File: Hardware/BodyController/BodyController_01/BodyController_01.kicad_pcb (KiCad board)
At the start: 4 copper layers, 155 x 106 mm, 407 parts, among them J1 7796, J10 Conn_01x01, J11 Conn_01x01, J12 Conn_01x01, J13 Conn_01x01, J2 Conn_01x14, J3 Conn_02x10_Top_Bottom, J4 Conn_02x10_Top_Bottom, J5 7796, J6 7796, J7 CONN_01X06, J8 USB_OTG, J9 Conn_01x01, Q1 NX1029X,115, Q10 NX1029X,115, Q12 BUK9Y3R0-40E,115, Q13 BUK9Y3R0-40E,115, Q16 2N7002, Q17 Q_PMOS_GSD, Q2 NX1029X,115, Q3 2N7002, Q4 SQJ423EP-T1_GE3, Q6 NX1029X,115, Q7 NX1029X,115, Q8 2N7002, Q9 2N7002, SW1 PTS645SM43SMTR92 LFS, U1 PIC33EPxxxMU810, U10 LM2904AVQDRQ1, U11 BTS50202EKAXUMA2, U12 BTS50202EKAXUMA2, U13 BTS50202EKAXUMA2, U14 OPA320-Q1, U15 BTS716G, U16 MCP2562-H/SN, U17 TPS70950QDBVRQ1, U18 TPS70933QDBVRQ1, U19 TPS70933QDBVRQ1, U2 LM2903QDRQ1, U20 LMR140x0, U21 LM2903QDRQ1, U22 DRV8872DDARQ1, U23 tps25940-q1, U25 UCC27511A-Q1, U27 INA21x, U29 FT230X, U3 INA21x, U4 BTS716G, U5 BTS500801TMAATMA1, U6 BTS500801TMAATMA1, U7 BTS50202EKAXUMA2, U8 BTS50202EKAXUMA2, U9 BTS50202EKAXUMA2, Y1 8MHz

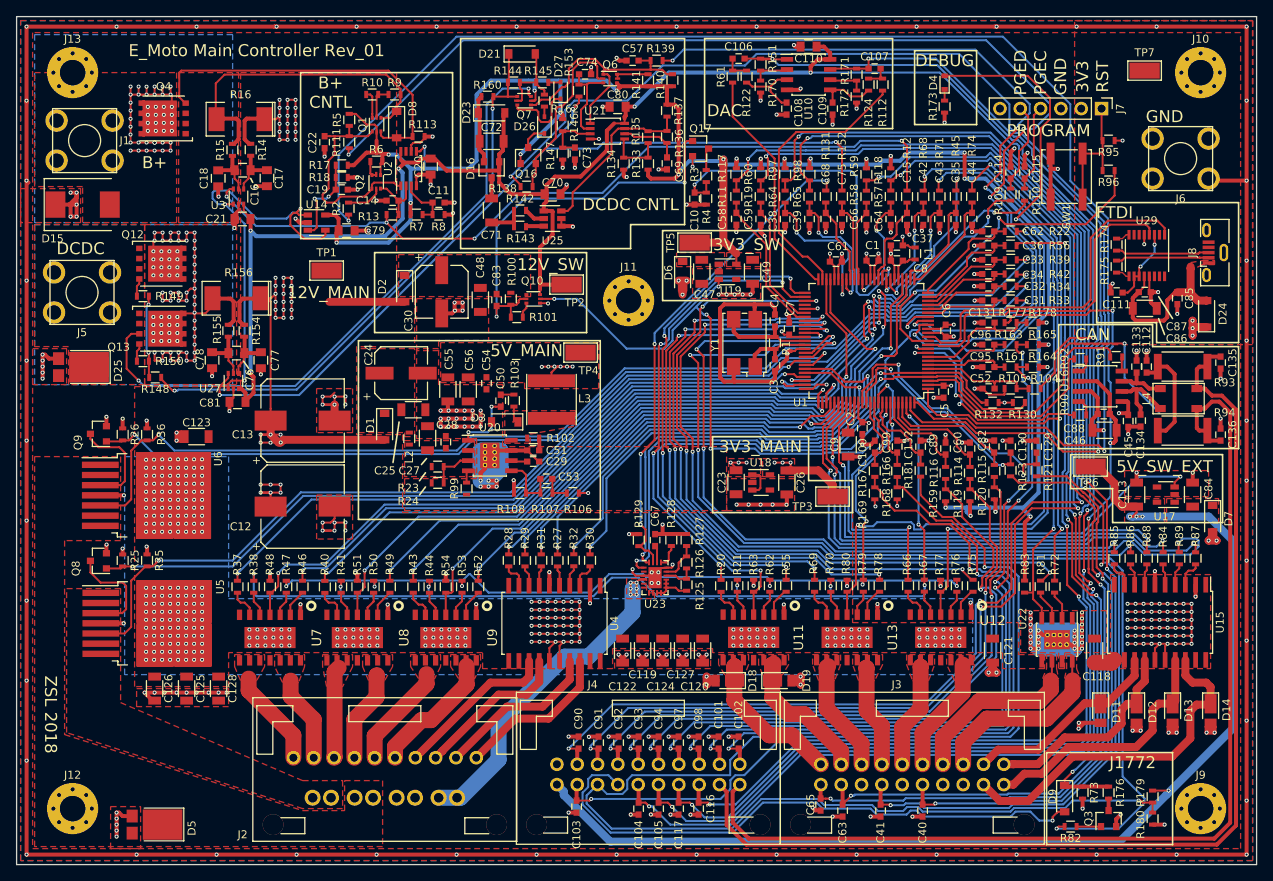
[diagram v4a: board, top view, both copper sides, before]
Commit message: Updated footprints, added CAN esd protection
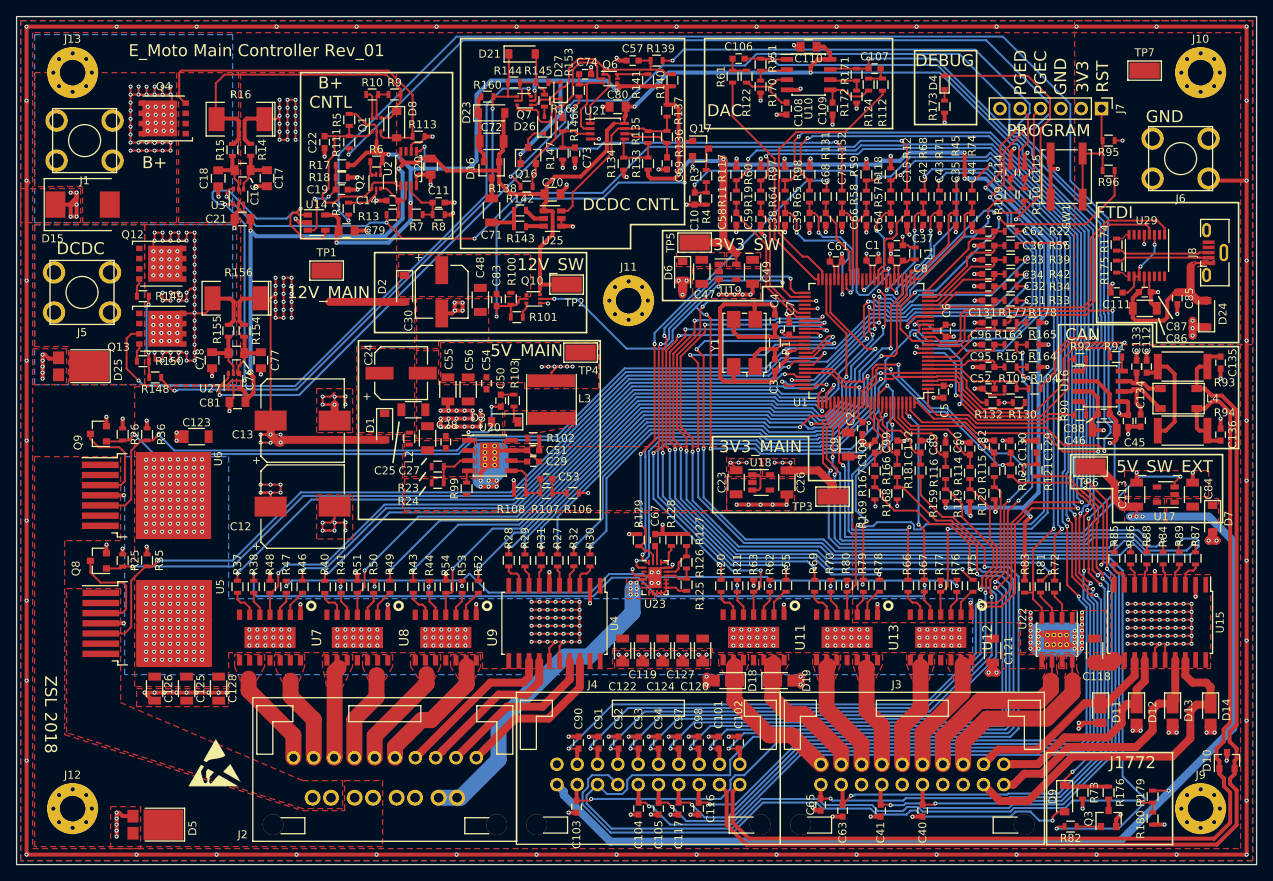
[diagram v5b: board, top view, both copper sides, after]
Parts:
- added D10: D_Schottky_x2_ACom_AKK, Footprints:D_SOT-23_ANK, F.Cu at (186.3, 150.0)
- added REF***: ESD-Logo_6.6x6mm_SilkScreen, Symbols:ESD-Logo_6.6x6mm_SilkScreen, F.Cu at (59.8, 150.2)
- Q12, Q13: value BUK9Y3R0-40E,115 -> BUK7J1R4-40HX
- moved D5 3.71 mm to (53.0, 158.0)
- moved D25 3.58 mm to (43.7, 100.7)
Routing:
- net (no net): track 22.5 -> 0.00 mm, vias 2 -> 0
- net +3V3: track 43.1 -> 64.3 mm, vias 16 -> 18
- net USB_5V: track 22.3 -> 24.8 mm
- net GND: track 986.5 -> 988.8 mm, vias 315 -> 316
- net CAN_P: track 135.7 -> 137.1 mm
- net CAN_N: track 132.1 -> 133.5 mm
- net BATT_EN: track 182.4 -> 183.4 mm

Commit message: Final layout for real this time. larger vias for EuroCircuit minimum rule.
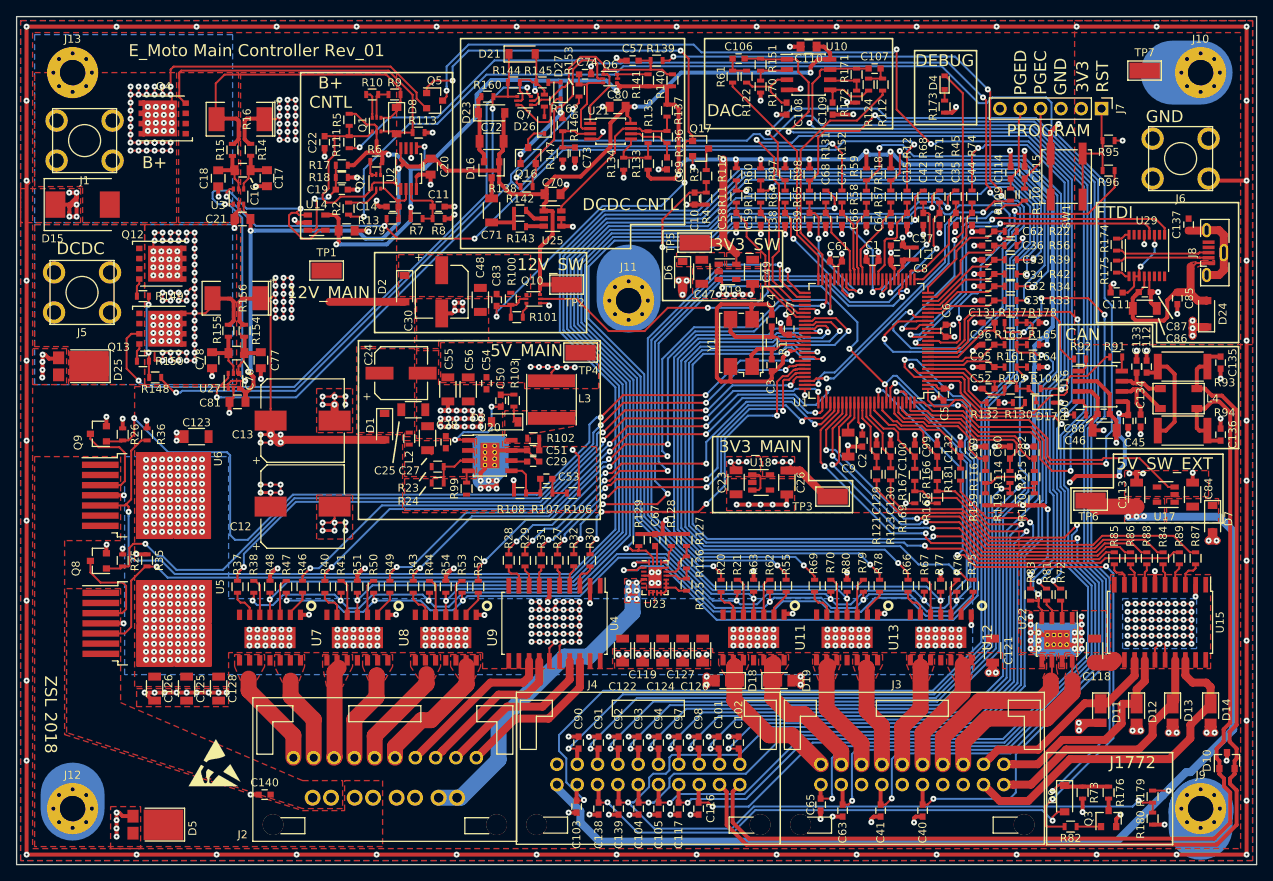
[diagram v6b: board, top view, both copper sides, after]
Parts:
- added C137: 10nF, Capacitors_SMD:C_0603, F.Cu at (181.5, 83.0)
- added C138: 10nF, Capacitors_SMD:C_0603, F.Cu at (107.8, 156.0)
- added C139: 10nF, Capacitors_SMD:C_0603, F.Cu at (110.2, 156.0)
- added C140: 10nF, Capacitors_SMD:C_0603, F.Cu at (66.0, 154.2)
- added D17: D_Schottky, Diodes_SMD:D_SOD-323, F.Cu at (163.5, 105.2)
- added Q5: Q_PMOS_GSD, TO_SOT_Packages_SMD:SOT-23, F.Cu at (87.2, 67.5)
- J10, J11, J12, J13, J9: footprint Mounting_Holes:MountingHole_3.2mm_M3_Pad_Via -> Footprints:MountingHole_3.2mm_M3_Pad_Via
- U2, U21: footprint Housings_SSOP:TSSOP-8_3x3mm_Pitch0.65mm -> Footprints:TSSOP-8_3x4.4mm_Pitch0.65mm
- moved C129 20.0 mm to (142.5, 111.2)
- moved R121 20.0 mm to (142.5, 114.2)
- moved C130 15.0 mm to (144.2, 111.2)
- moved R123 15.0 mm to (144.2, 114.2)
- moved C82 5.06 mm to (162.2, 111.5)
- moved R115 5.06 mm to (162.2, 114.5)
- moved R120 5.06 mm to (162.2, 117.3)
- moved C100 5.02 mm to (147.3, 111.3)
- moved C132 5.02 mm to (153.0, 111.2)
- moved C60 5.02 mm to (159.2, 111.5)
- moved C89 5.02 mm to (156.1, 111.5)
- moved C99 5.02 mm to (150.1, 111.2)
- moved R114 5.02 mm to (159.2, 114.5)
- moved R116 5.02 mm to (156.1, 114.5)
- moved R119 5.02 mm to (159.2, 117.3)
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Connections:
- J10 pad 1: Net-(J10-Pad1) -> GND
- J11 pad 1: Net-(J11-Pad1) -> GND
- J12 pad 1: Net-(J12-Pad1) -> GND
- J13 pad 1: Net-(J13-Pad1) -> GND
- J4 pad 13: PROXIMITY -> PILOT
- J4 pad 14: PILOT -> PROXIMITY
- J8 pad 6: GND -> Net-(C137-Pad1)
- J9 pad 1: Net-(J9-Pad1) -> GND
- R104 pad 1: +12P -> Net-(Q5-Pad3)
- U1 pad 59: PILOT_EN -> J1772_CONTROLLER_EN
- U1 pad 68: AUX_PORT_EN -> HORN_EN
- U1 pad 69: HORN_EN -> AUX_PORT_EN
- U1 pad 91: J1772_CONTROLLER_EN -> PILOT_EN
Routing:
- net Net-(Q5-Pad3): track 0.00 -> 124.6 mm, vias 0 -> 4
- net Net-(R34-Pad1): track 133.9 -> 201.7 mm
- net +12P: track 221.9 -> 155.4 mm, vias 6 -> 5
- net PILOT_EN: track 142.5 -> 85.1 mm
- net Net-(R33-Pad1): track 137.9 -> 193.0 mm
- net GND: track 988.8 -> 1040.0 mm, vias 316 -> 312
- net Net-(R68-Pad1): track 81.6 -> 126.3 mm
- net J1772_CONTROLLER_EN: track 36.9 -> 79.3 mm
- net Net-(R42-Pad1): track 110.5 -> 152.7 mm, vias 4 -> 2
- net Net-(R39-Pad1): track 121.3 -> 163.0 mm, vias 4 -> 2
- net DIVIDER_EN: track 50.1 -> 91.1 mm, vias 2 -> 4
- net +BATT: track 29.8 -> 66.7 mm
- net IC_CONTROLLER_SLEEP: track 72.6 -> 105.5 mm
- net IC_CONTROLLER_~FLT: track 66.4 -> 96.4 mm
- net CHARGE_PORT_RELEASE_EN: track 92.7 -> 120.0 mm, vias 4 -> 2
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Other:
- net class 5A: via_dia 0.5 -> 0.75
- net class Default: via_dia 0.5 -> 0.75
- net class GND: via_dia 0.5 -> 0.75
- rule via_min_size: 0.5 -> 0.75
